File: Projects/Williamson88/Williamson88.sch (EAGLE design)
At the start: 36 parts

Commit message: Created library for audio transformer
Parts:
- added U$1: CXPP30, CXPP30:CXPP30
- added U$10, U$11, U$12, U$13, U$14, U$15, U$2, U$3, U$4, U$5, U$6, U$7, U$8, U$9: W_CONN, CXPP30:W_CONN
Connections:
- removed net FB: CY3.2, R22.2
- new net 16O: CY3.2, R22.2, U$6.P$1
- new net 4O: U$8.P$1
- new net 8O: U$7.P$1
- new net COMMON: U$9.P$1
- net -80V: now also U$10.P$1
- net 230V: now also U$11.P$1
- net 320V: now also U$12.P$1
- net 477V: now also U$13.P$1
- net HEATERS_M: now also U$15.P$1
- net HEATERS_P: now also U$14.P$1
- net T1A: now also U$2.P$1
- net T2A: now also U$3.P$1
- net T3A: now also U$4.P$1
- net T4A: now also U$5.P$1
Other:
- moved on the sheet: V1", V2", V3", V4"

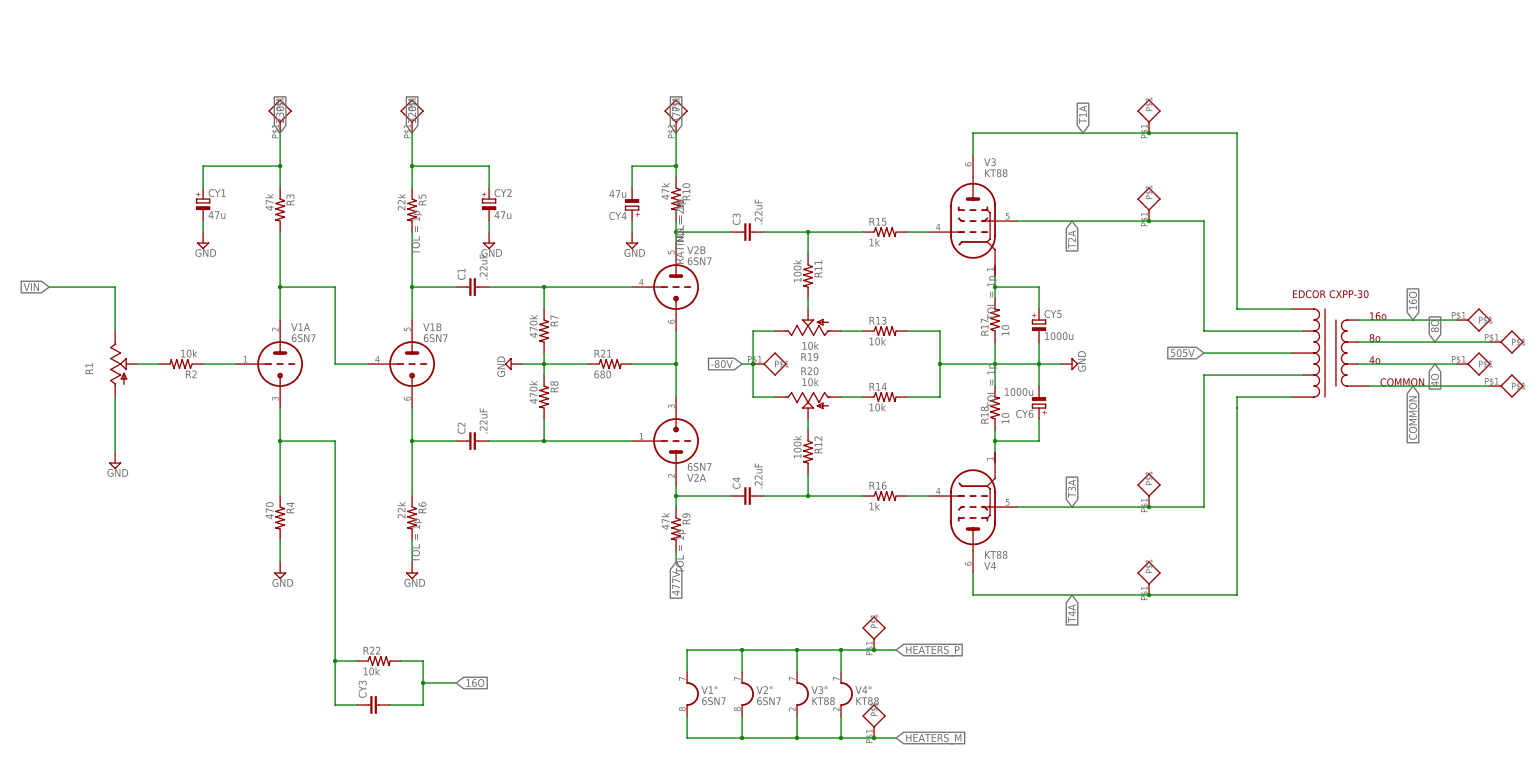
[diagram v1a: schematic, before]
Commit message: Added library for audio caps
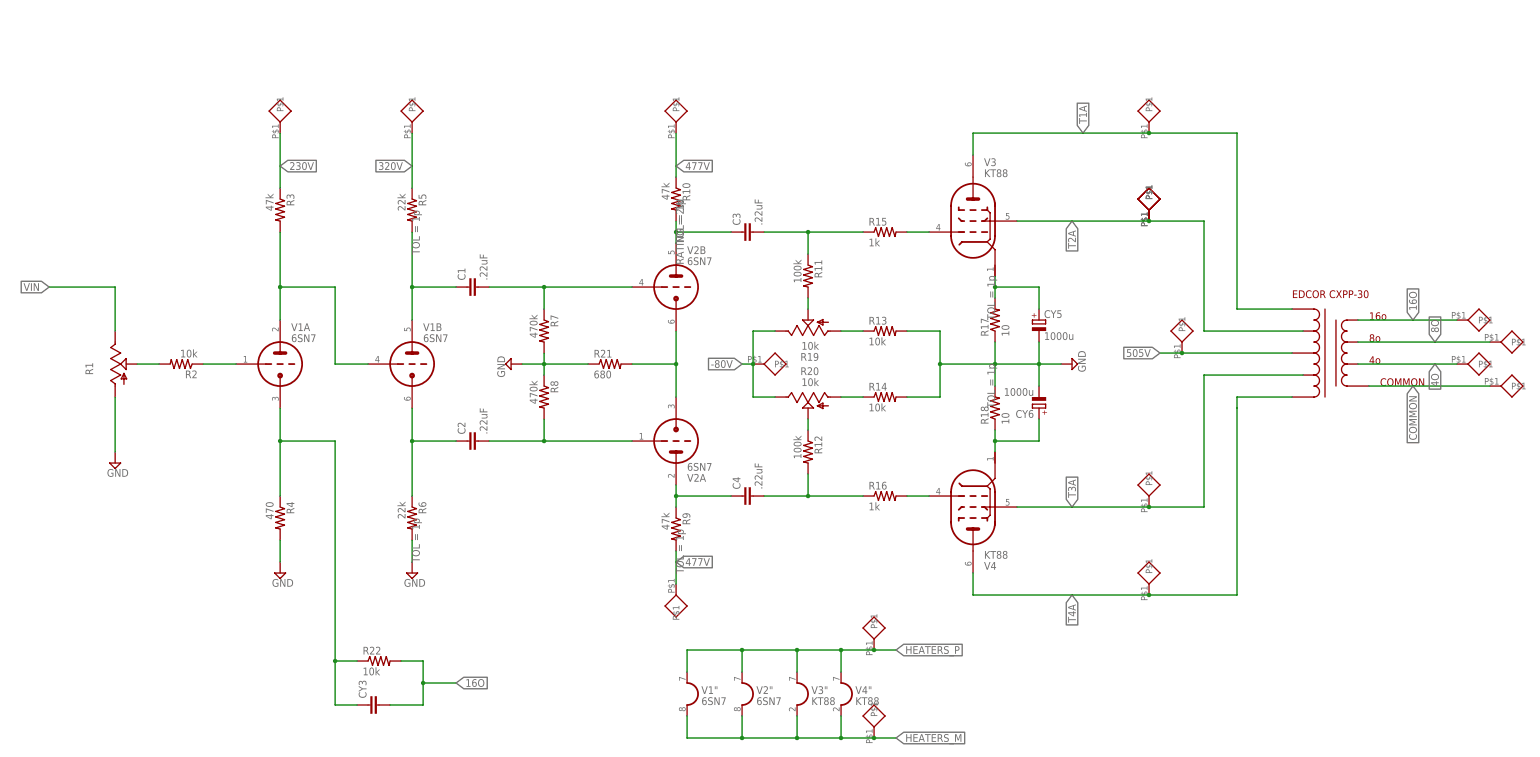
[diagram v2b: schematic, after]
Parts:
- removed CY1, CY2, CY4: 47u, rcl:CPOL-EUE7.5-18
- added U$16, U$17, U$18: W_CONN, CXPP30:W_CONN
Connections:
- new net 505V: U$18.P$1
- net 230V: no longer CY1.+
- net 320V: no longer CY2.+
- net 477V: now also U$16.P$1; no longer CY4.-
- net GND: no longer CY1.-, CY2.-, CY4.+
- net T2A: now also U$17.P$1
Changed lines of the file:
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@@
 </variantdefs>
 <classes>
-<class number="0" name="default" width="0" drill="0">
+<class number="0" name="default" width="0.2032" drill="0.254">
+<clearance class="0" value="0.254"/>
+</class>
+<class number="1" name="LV" width="0.889" drill="0.889">
+<clearance class="1" value="0.889"/>
 </class>
 </classes>
@@
 <part name="V2" library="tubes" deviceset="6SN7GT-P" device="" value="6SN7"/>
 <part name="R22" library="rcl" deviceset="R-US_" device="0309/10" value="10k"/>
-<part name="CY1" library="rcl" deviceset="CPOL-EU" device="E7.5-18" value="47u">
-<attribute name="RATING" value="275V"/>
-</part>
-<part name="CY2" library="rcl" deviceset="CPOL-EU" device="E7.5-18" value="47u">
-<attribute name="RATING" value="375V"/>
-</part>
 <part name="CY3" library="rcl" deviceset="CY" device="YC10B5"/>
-<part name="CY4" library="rcl" deviceset="CPOL-EU" device="E7.5-18" value="47u">
-<attribute name="RATING" value="630V"/>
-</part>
-<part name="SUPPLY6" library="supply2" deviceset="GND" device=""/>
-<part name="SUPPLY7" library="supply2" deviceset="GND" device=""/>
-<part name="SUPPLY8" library="supply2" deviceset="GND" device=""/>
 <part name="CY5" library="rcl" deviceset="CPOL-EU" device="E7.5-18" value="1000u">
 <attribute name="RATING" value="50V"/>
@@
 <part name="U$14" library="CXPP30" deviceset="W_CONN" device=""/>
 <part name="U$15" library="CXPP30" deviceset="W_CONN" device=""/>
+<part name="U$16" library="CXPP30" deviceset="W_CONN" device=""/>
+<part name="U$17" library="CXPP30" deviceset="W_CONN" device=""/>
+<part name="U$18" library="CXPP30" deviceset="W_CONN" device=""/>
 </parts>
 <sheets>
@@
 <instance part="V1" gate="&quot;" x="63.5" y="-81.28"/>
 <instance part="R22" gate="G$1" x="-7.62" y="-68.58"/>
-<instance part="CY1" gate="G$1" x="-48.26" y="38.1">
-<attribute name="RATING" x="-48.26" y="38.1" size="1.778" layer="96" display="off"/>
-</instance>
-<instance part="CY2" gate="G$1" x="17.78" y="38.1">
-<attribute name="RATING" x="17.78" y="38.1" size="1.778" layer="96" display="off"/>
-</instance>
 <instance part="CY3" gate="G$1" x="-10.16" y="-78.74" rot="R90"/>
-<instance part="CY4" gate="G$1" x="50.8" y="35.56" rot="R180">
-<attribute name="RATING" x="50.8" y="35.56" size="1.778" layer="96" rot="R180" display="off"/>
-</instance>
-<instance part="SUPPLY6" gate="GND" x="-48.26" y="27.94"/>
-<instance part="SUPPLY7" gate="GND" x="17.78" y="27.94"/>
-<instance part="SUPPLY8" gate="GND" x="50.8" y="27.94"/>
 <instance part="CY5" gate="G$1" x="144.78" y="10.16">
 <attribute name="RATING" x="144.78" y="10.16" size="1.778" layer="96" display="off"/>
@@
 <instance part="U$14" gate="G$1" x="106.68" y="-66.04"/>
 <instance part="U$15" gate="G$1" x="106.68" y="-86.36"/>
+<instance part="U$16" gate="G$1" x="60.96" y="-50.8" rot="R180"/>
+<instance part="U$17" gate="G$1" x="170.18" y="33.02"/>
+<instance part="U$18" gate="G$1" x="177.8" y="2.54"/>
 </instances>
 <busses>
@@
 <wire x1="-68.58" y1="-7.62" x2="-68.58" y2="-20.32" width="0.1524" layer="91"/>
 </segment>
-<segment>
-<pinref part="CY4" gate="G$1" pin="+"/>
-<pinref part="SUPPLY8" gate="GND" pin="GND"/>
-<wire x1="50.8" y1="33.02" x2="50.8" y2="30.48" width="0.1524" layer="91"/>
-</segment>
-<segment>
-<pinref part="CY2" gate="G$1" pin="-"/>
-<pinref part="SUPPLY7" gate="GND" pin="GND"/>
-<wire x1="17.78" y1="33.02" x2="17.78" y2="30.48" width="0.1524" layer="91"/>
-</segment>
-<segment>
-<pinref part="CY1" gate="G$1" pin="-"/>
-<pinref part="SUPPLY6" gate="GND" pin="GND"/>
-<wire x1="-48.26" y1="33.02" x2="-48.26" y2="30.48" width="0.1524" layer="91"/>
-</segment>
 </net>
 <net name="230V" class="0">
@@
 <pinref part="R3" gate="G$1" pin="1"/>
 <wire x1="-30.48" y1="40.64" x2="-30.48" y2="45.72" width="0.1524" layer="91"/>
-<label x="-30.48" y="53.34" size="1.778" layer="95" rot="R90" xref="yes"/>
-<pinref part="CY1" gate="G$1" pin="+"/>
 <wire x1="-30.48" y1="45.72" x2="-30.48" y2="53.34" width="0.1524" layer="91"/>
-<wire x1="-48.26" y1="40.64" x2="-48.26" y2="45.72" width="0.1524" layer="91"/>
-<wire x1="-48.26" y1="45.72" x2="-30.48" y2="45.72" width="0.1524" layer="91"/>
-<junction x="-30.48" y="45.72"/>
 <pinref part="U$11" gate="G$1" pin="P$1"/>
+<label x="-30.48" y="45.72" size="1.778" layer="95" xref="yes"/>
 </segment>
 </net>
@@
 <pinref part="R5" gate="G$1" pin="1"/>
 <wire x1="0" y1="40.64" x2="0" y2="45.72" width="0.1524" layer="91"/>
-<label x="0" y="53.34" size="1.778" layer="95" rot="R90" xref="yes"/>
-<pinref part="CY2" gate="G$1" pin="+"/>
 <wire x1="0" y1="45.72" x2="0" y2="53.34" width="0.1524" layer="91"/>
-<wire x1="0" y1="45.72" x2="17.78" y2="45.72" width="0.1524" layer="91"/>
-<wire x1="17.78" y1="45.72" x2="17.78" y2="40.64" width="0.1524" layer="91"/>
-<junction x="0" y="45.72"/>
 <pinref part="U$12" gate="G$1" pin="P$1"/>
+<label x="0" y="45.72" size="1.778" layer="95" rot="R180" xref="yes"/>
 </segment>
 </net>
@@
 <pinref part="R10" gate="G$1" pin="1"/>
 <wire x1="60.96" y1="43.18" x2="60.96" y2="45.72" width="0.1524" layer="91"/>
-<label x="60.96" y="53.34" size="1.778" layer="95" rot="R90" xref="yes"/>
-<pinref part="CY4" gate="G$1" pin="-"/>
 <wire x1="60.96" y1="45.72" x2="60.96" y2="53.34" width="0.1524" layer="91"/>
-<wire x1="50.8" y1="40.64" x2="50.8" y2="45.72" width="0.1524" layer="91"/>
-<wire x1="50.8" y1="45.72" x2="60.96" y2="45.72" width="0.1524" layer="91"/>
-<junction x="60.96" y="45.72"/>
 <pinref part="U$13" gate="G$1" pin="P$1"/>
+<label x="60.96" y="45.72" size="1.778" layer="95" xref="yes"/>
 </segment>
 <segment>
 <pinref part="R9" gate="G$1" pin="2"/>
 <wire x1="60.96" y1="-43.18" x2="60.96" y2="-45.72" width="0.1524" layer="91"/>
-<label x="60.96" y="-45.72" size="1.778" layer="95" rot="R270" xref="yes"/>
-</segment>
-</net>
-<net name="N$8" class="0">
+<label x="60.96" y="-45.72" size="1.778" layer="95" xref="yes"/>
+<wire x1="60.96" y1="-45.72" x2="60.96" y2="-50.8" width="0.1524" layer="91"/>
+<pinref part="U$16" gate="G$1" pin="P$1"/>
+</segment>
+</net>
+<net name="N$8" class="1">
 <segment>
 <pinref part="R1" gate="G$1" pin="S"/>
@@
 </segment>
 </net>
-<net name="N$19" class="0">
+<net name="N$19" class="1">
 <segment>
 <pinref part="R2" gate="G$1" pin="1"/>
@@
 </segment>
 </net>
-<net name="VIN" class="0">
+<net name="VIN" class="1">
 <segment>
 <pinref part="R1" gate="G$1" pin="E"/>
@@
 <pinref part="U$3" gate="G$1" pin="P$1"/>
 <junction x="170.18" y="33.02"/>
+<pinref part="U$17" gate="G$1" pin="P$1"/>
 </segment>
 </net>
@@
 <net name="505V" class="0">
 <segment>
-<wire x1="203.2" y1="2.54" x2="182.88" y2="2.54" width="0.1524" layer="91"/>
-<label x="182.88" y="2.54" size="1.778" layer="95" rot="R180" xref="yes"/>
-</segment>
-</net>
+<wire x1="203.2" y1="2.54" x2="177.8" y2="2.54" width="0.1524" layer="91"/>
+<label x="172.72" y="2.54" size="1.778" layer="95" rot="R180" xref="yes"/>
+<pinref part="U$18" gate="G$1" pin="P$1"/>
+<wire x1="177.8" y1="2.54" x2="172.72" y2="2.54" width="0.1524" layer="91"/>
+<junction x="177.8" y="2.54"/>
+</segment>
+</net>

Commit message: Cleanup and schematic for the amplifier part
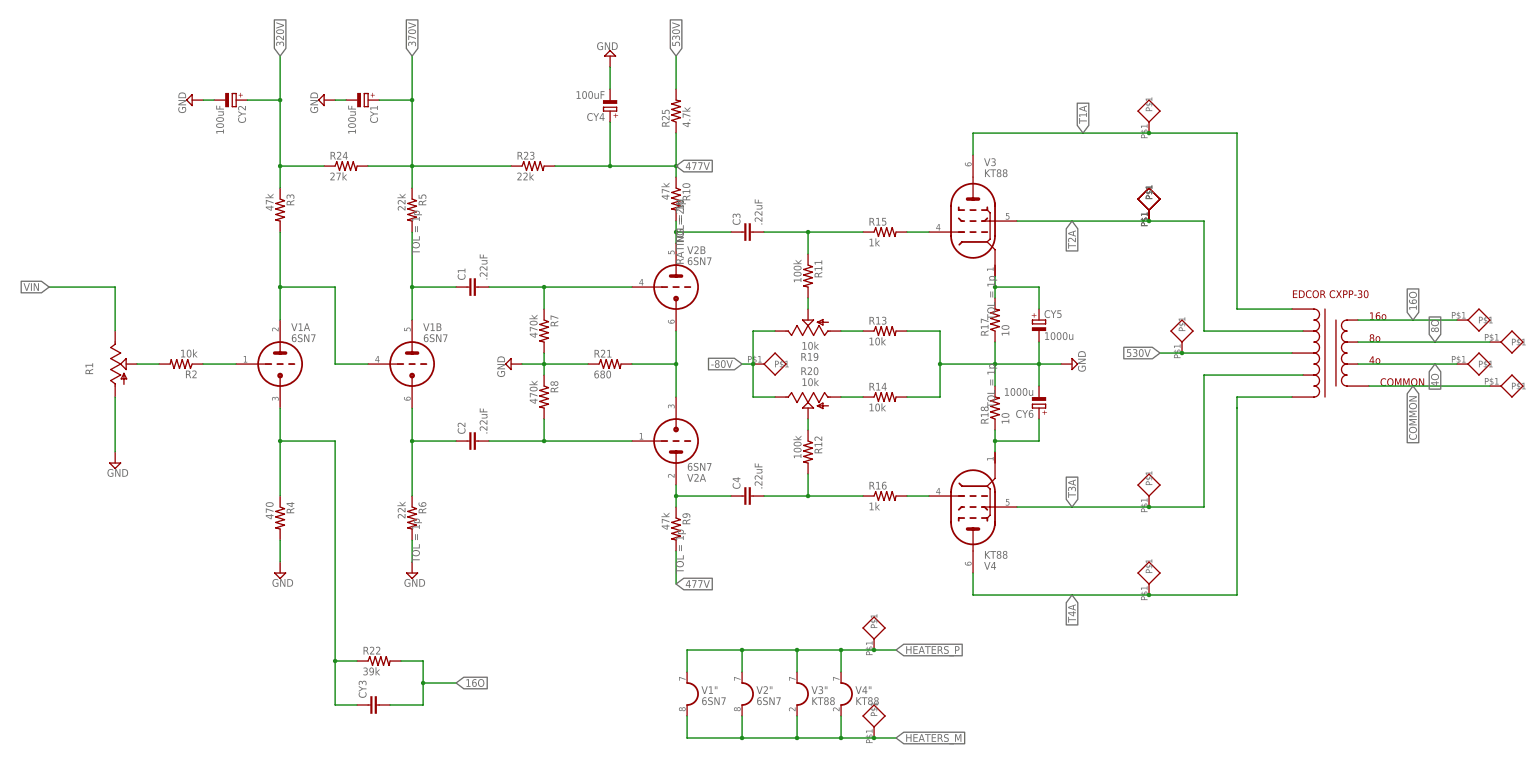
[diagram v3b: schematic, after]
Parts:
- removed U$11, U$12, U$13, U$16: W_CONN, CXPP30:W_CONN
- added CY1, CY2, CY4: 100uF, rcl:CPOL-EUE7.5-18
- added R23: 22k, rcl:R-US_0309/10
- added R24: 27k, rcl:R-US_0309/10
- added R25: 4.7k, rcl:R-US_0309/10
- R22: value 10k -> 39k
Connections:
- removed net 230V: R3.1, U$11.P$1
- removed net 505V: U$18.P$1
- new net 370V: CY1.+, R23.1, R24.2, R5.1
- new net 530V: R25.2, U$18.P$1
- net 320V: now also CY2.+, R24.1, R3.1; no longer R5.1, U$12.P$1
- net 477V: now also CY4.+, R23.2, R25.1; no longer U$13.P$1, U$16.P$1
- net GND: now also CY1.-, CY2.-, CY4.-
